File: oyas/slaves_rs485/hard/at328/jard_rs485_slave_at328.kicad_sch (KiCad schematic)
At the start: 60 parts, among them J1 POWER, J7 ISCP, U1 BPC_Alim5V, U1 MAX485E, U2 ATmega328P-A, Y1 8MHz

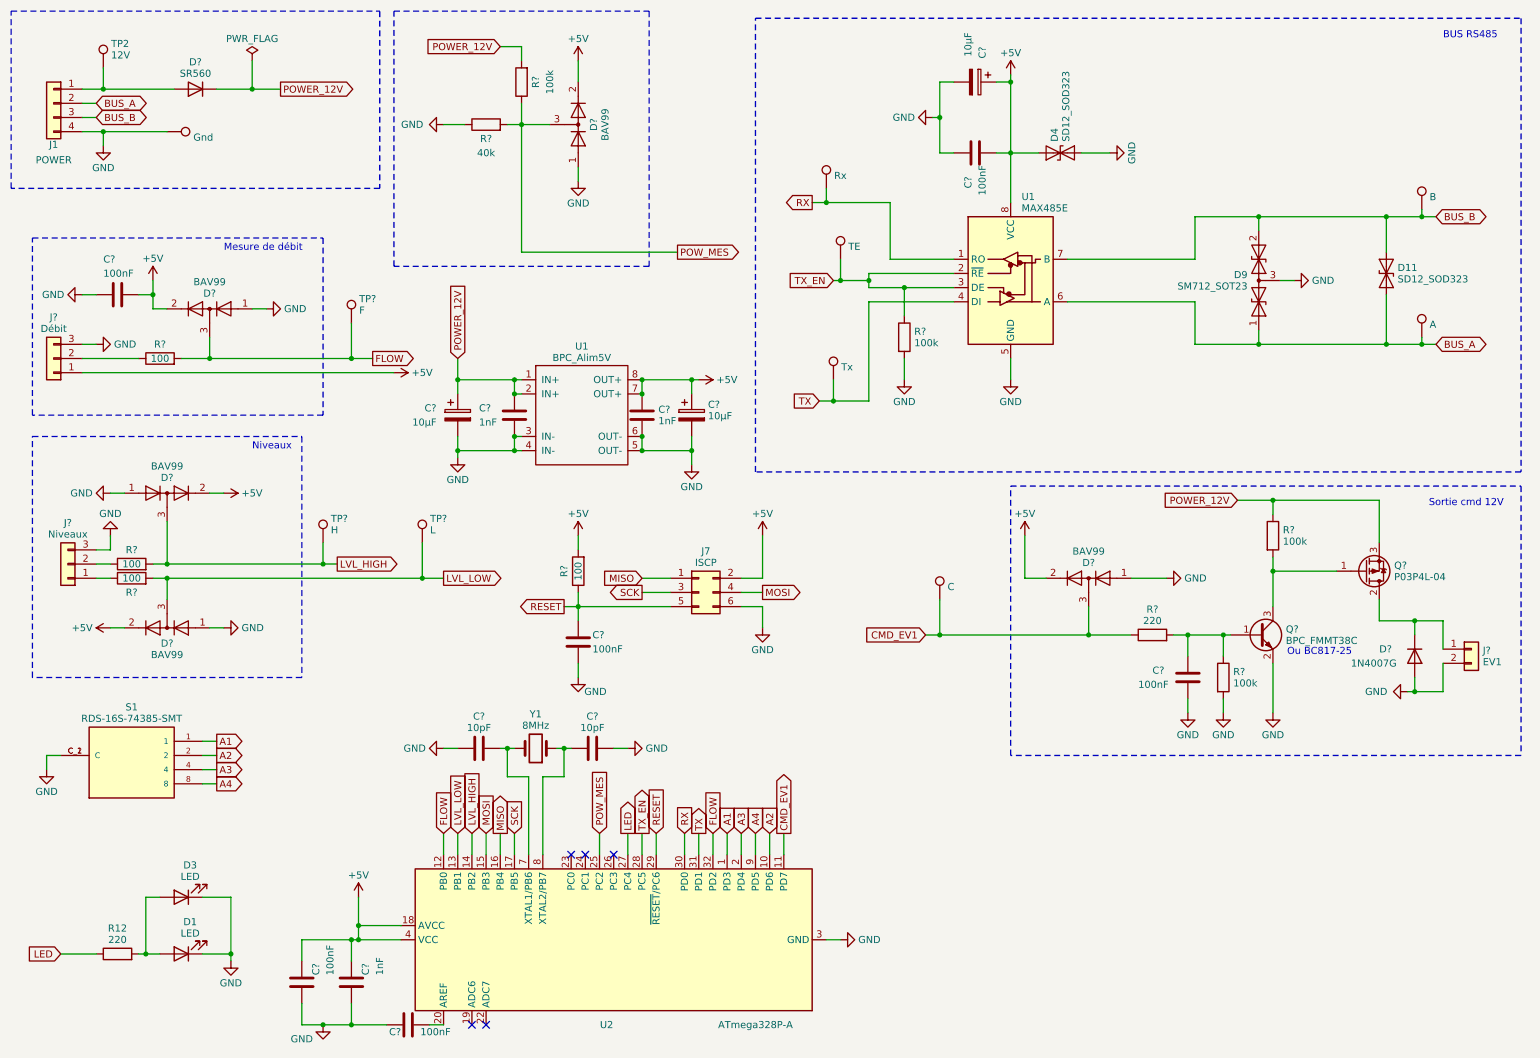
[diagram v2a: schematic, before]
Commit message: Améliorations sur carte AT328
- Capas en hand soldering et en 805
- TP + gros
- Repères composants
- Carte moins longue
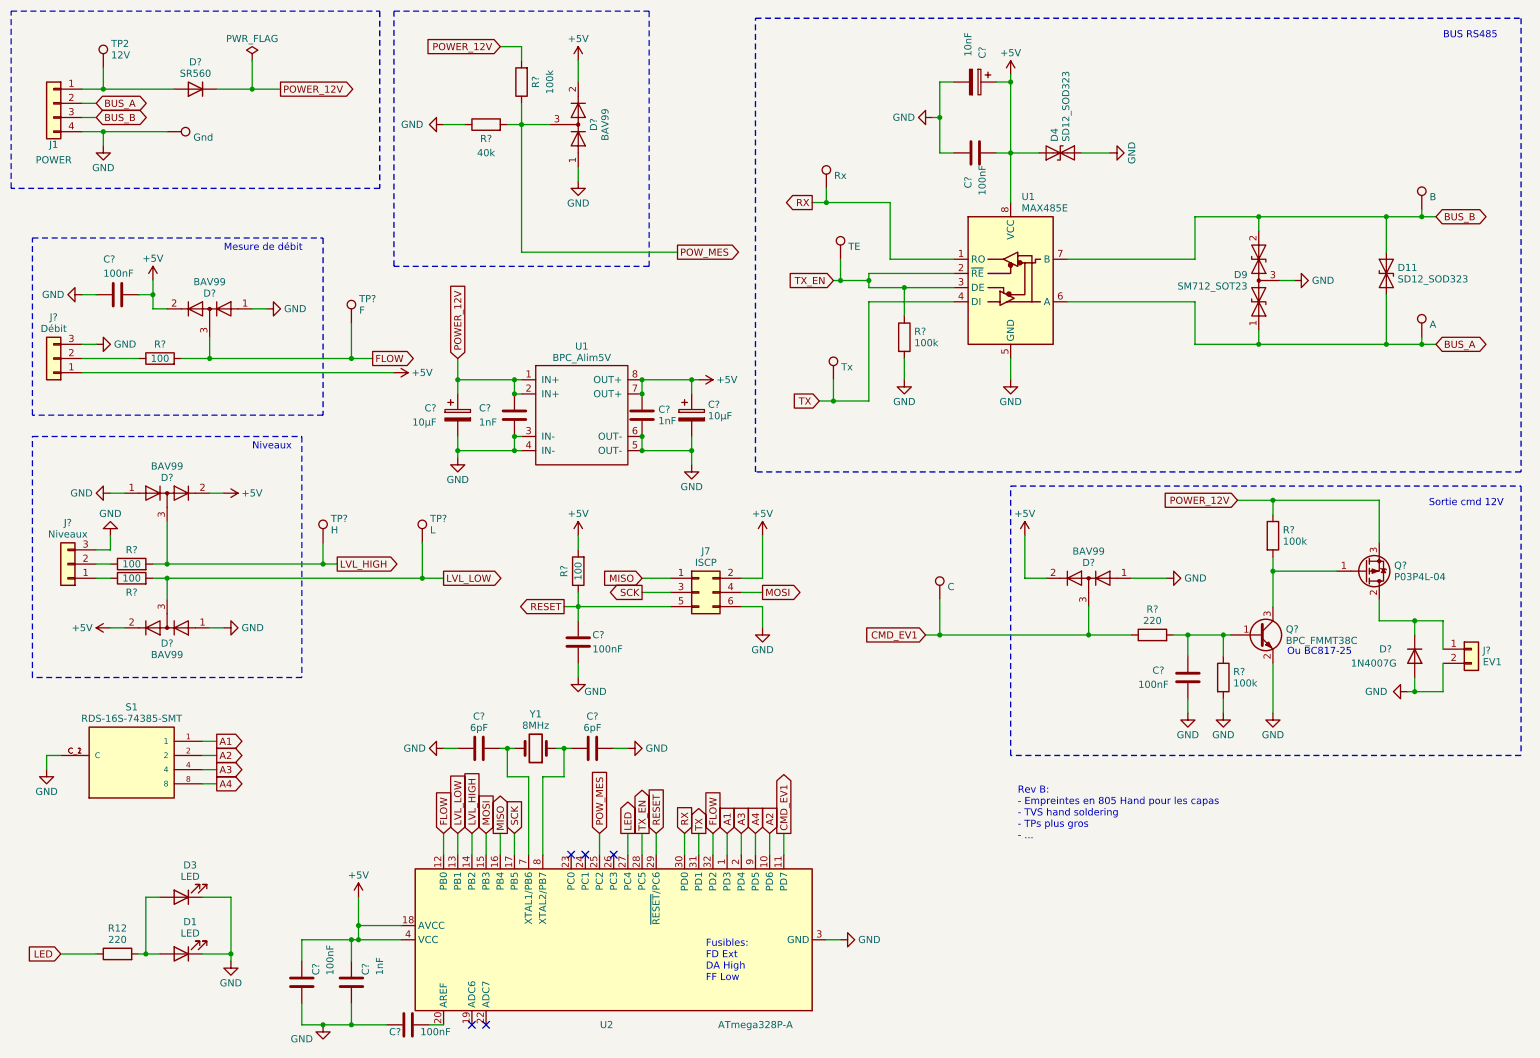
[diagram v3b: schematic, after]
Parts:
- C? (x6): footprint Capacitor_SMD:C_0805_2012Metric -> Capacitor_SMD:C_0805_2012Metric_Pad1.18x1.45mm_HandSolder
- C? (x2): footprint Capacitor_SMD:C_0603_1608Metric -> Capacitor_SMD:C_0805_2012Metric_Pad1.18x1.45mm_HandSolder
- C? (x2): value 10pF -> 6pF; footprint Capacitor_SMD:C_0603_1608Metric -> Capacitor_SMD:C_0603_1608Metric_Pad1.08x0.95mm_HandSolder
- C?: value 10µF -> 10nF; footprint Capacitor_SMD:C_0805_2012Metric -> Capacitor_SMD:C_0805_2012Metric_Pad1.18x1.45mm_HandSolder
- TP1, TP2, TP3, TP4, TP5, TP? (x4): footprint TestPoint:TestPoint_Pad_D1.0mm -> TestPoint:TestPoint_Pad_D2.0mm
- U1: Fabricant (none) -> Analog Devices; Fournisseur (none) -> Farnell; RefFabricant (none) -> MAX485ESA+; RefFournisseur (none) -> 2519382
- U2: Fabricant (none) -> MICROCHIP; Fournisseur (none) -> Farnell; RefFabricant (none) -> ATMEGA328P-AU; RefFournisseur (none) -> 1715486
- Y1: Fabricant (none) -> Abracon; Farnel 4242855 -> (none); Fournisseur (none) -> Farnell; RefFab ABM8AAIG-8.000MHZ-V2R-T3 -> (none); RefFabricant (none) -> ABM8AAIG-8.000MHZ-V2R-T3; RefFournisseur (none) -> 4242855
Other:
- note added: "Fusibles: FD Ext DA High FF Low"
- note added: "Rev B: - Empreintes en 805 Hand pour les capas - TVS hand soldering - TPs plus gros - ..."
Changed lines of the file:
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@@
     (effects (font (size 1.27 1.27)) (justify left bottom))
   )
+  (text "Fusibles:\nFD Ext\nDA High\nFF Low" (at 137.16 186.69 0)
+    (effects (font (size 1.27 1.27)) (justify left bottom))
+  )
   (text "Sortie cmd 12V" (at 266.7 101.6 0)
     (effects (font (size 1.27 1.27)) (justify left bottom))
@@
     (effects (font (size 1.27 1.27)) (justify left bottom))
   )
+  (text "Rev B:\n- Empreintes en 805 Hand pour les capas\n- TVS hand soldering\n- TPs plus gros\n- ..."
+    (at 193.04 161.29 0)
+    (effects (font (size 1.27 1.27)) (justify left bottom))
+  )
   (global_label "LED" (shape output) (at 123.19 160.02 90) (fields_autoplaced)
     (effects (font (size 1.27 1.27)) (justify left))
@@
       (effects (font (size 1.27 1.27)) (justify left))
     )
-    (property "Footprint" "Capacitor_SMD:C_0805_2012Metric" (at 87.63 193.3448 0)
+    (property "Footprint" "Capacitor_SMD:C_0805_2012Metric_Pad1.18x1.45mm_HandSolder" (at 87.63 193.3448 0)
       (effects (font (size 1.27 1.27)) hide)
     )
@@
       (effects (font (size 1.27 1.27)) (justify left))
     )
-    (property "Footprint" "Capacitor_SMD:C_0805_2012Metric" (at 224.4852 135.89 0)
+    (property "Footprint" "Capacitor_SMD:C_0805_2012Metric_Pad1.18x1.45mm_HandSolder" (at 224.4852 135.89 0)
       (effects (font (size 1.27 1.27)) hide)
     )
@@
       (effects (font (size 1.27 1.27)) (justify left))
     )
-    (property "Footprint" "TestPoint:TestPoint_Pad_D1.0mm" (at 78.74 68.58 0)
+    (property "Footprint" "TestPoint:TestPoint_Pad_D2.0mm" (at 78.74 68.58 0)
       (effects (font (size 1.27 1.27)) hide)
     )
@@
       (effects (font (size 1.27 1.27)) (justify left))
     )
-    (property "Footprint" "Capacitor_SMD:C_0805_2012Metric" (at 115.2652 129.54 0)
+    (property "Footprint" "Capacitor_SMD:C_0805_2012Metric_Pad1.18x1.45mm_HandSolder" (at 115.2652 129.54 0)
       (effects (font (size 1.27 1.27)) hide)
     )
@@
       (effects (font (size 1.27 1.27)) (justify left))
     )
-    (property "Footprint" "Capacitor_SMD:C_0805_2012Metric" (at 65.7352 190.5 0)
+    (property "Footprint" "Capacitor_SMD:C_0805_2012Metric_Pad1.18x1.45mm_HandSolder" (at 65.7352 190.5 0)
       (effects (font (size 1.27 1.27)) hide)
     )
@@
       (effects (font (size 1.27 1.27)) (justify left))
     )
-    (property "Footprint" "Capacitor_SMD:C_0603_1608Metric" (at 126.6952 88.9 0)
+    (property "Footprint" "Capacitor_SMD:C_0805_2012Metric_Pad1.18x1.45mm_HandSolder" (at 126.6952 88.9 0)
       (effects (font (size 1.27 1.27)) hide)
     )
@@
       (effects (font (size 1.27 1.27)) (justify left))
     )
-    (property "Footprint" "TestPoint:TestPoint_Pad_D1.0mm" (at 165.1 78.74 0)
+    (property "Footprint" "TestPoint:TestPoint_Pad_D2.0mm" (at 165.1 78.74 0)
       (effects (font (size 1.27 1.27)) hide)
     )
@@
       (effects (font (size 1.27 1.27)) (justify left))
     )
-    (property "Footprint" "TestPoint:TestPoint_Pad_D1.0mm" (at 34.29 22.86 0)
+    (property "Footprint" "TestPoint:TestPoint_Pad_D2.0mm" (at 34.29 22.86 0)
       (effects (font (size 1.27 1.27)) hide)
     )
@@
       (effects (font (size 1.27 1.27)) (justify left))
     )
-    (property "Footprint" "TestPoint:TestPoint_Pad_D1.0mm" (at 91.44 107.95 0)
+    (property "Footprint" "TestPoint:TestPoint_Pad_D2.0mm" (at 91.44 107.95 0)
       (effects (font (size 1.27 1.27)) hide)
     )
@@
       (effects (font (size 1.27 1.27)) (justify left))
     )
-    (property "Footprint" "TestPoint:TestPoint_Pad_D1.0mm" (at 40.64 39.37 0)
+    (property "Footprint" "TestPoint:TestPoint_Pad_D2.0mm" (at 40.64 39.37 0)
       (effects (font (size 1.27 1.27)) hide)
     )
@@
       (effects (font (size 1.27 1.27)) (justify left))
     )
-    (property "Footprint" "TestPoint:TestPoint_Pad_D1.0mm" (at 73.66 107.95 0)
+    (property "Footprint" "TestPoint:TestPoint_Pad_D2.0mm" (at 73.66 107.95 0)
       (effects (font (size 1.27 1.27)) hide)
     )
@@
       (effects (font (size 1.27 1.27)) (justify left))
     )
-    (property "Footprint" "TestPoint:TestPoint_Pad_D1.0mm" (at 270.51 71.12 0)
+    (property "Footprint" "TestPoint:TestPoint_Pad_D2.0mm" (at 270.51 71.12 0)
       (effects (font (size 1.27 1.27)) hide)
     )
@@
       (effects (font (size 1.27 1.27)))
     )
-    (property "Value" "10pF" (at 96.52 141.089 90)
+    (property "Value" "6pF" (at 96.52 141.089 90)
       (effects (font (size 1.27 1.27)))
     )
-    (property "Footprint" "Capacitor_SMD:C_0603_1608Metric" (at 100.33 143.8148 0)
+    (property "Footprint" "Capacitor_SMD:C_0603_1608Metric_Pad1.08x0.95mm_HandSolder" (at 100.33 143.8148 0)
       (effects (font (size 1.27 1.27)) hide)
     )
@@
       (effects (font (size 1.27 1.27)) hide)
     )
+    (property "Fabricant" "MICROCHIP" (at 120.65 179.07 0)
+      (effects (font (size 1.27 1.27)) hide)
+    )
+    (property "Fournisseur" "Farnell" (at 120.65 179.07 0)
+      (effects (font (size 1.27 1.27)) hide)
+    )
+    (property "RefFabricant" "ATMEGA328P-AU" (at 120.65 179.07 0)
+      (effects (font (size 1.27 1.27)) hide)
+    )
+    (property "RefFournisseur" "1715486" (at 120.65 179.07 0)
+      (effects (font (size 1.27 1.27)) hide)
+    )
     (pin "1")
     (pin "10")
@@
       (effects (font (size 1.27 1.27)) (justify left))
     )
-    (property "Footprint" "TestPoint:TestPoint_Pad_D1.0mm" (at 184.15 118.11 0)
+    (property "Footprint" "TestPoint:TestPoint_Pad_D2.0mm" (at 184.15 118.11 0)
       (effects (font (size 1.27 1.27)) hide)
     )
@@
       (effects (font (size 1.27 1.27)) (justify left))
     )
-    (property "Value" "10µF" (at 184.15 16.51 0)
+    (property "Value" "10nF" (at 184.15 16.51 0)
       (effects (font (size 1.27 1.27)) (justify left))
     )
-    (property "Footprint" "Capacitor_SMD:C_0805_2012Metric" (at 181.61 26.3652 0)
+    (property "Footprint" "Capacitor_SMD:C_0805_2012Metric_Pad1.18x1.45mm_HandSolder" (at 181.61 26.3652 0)
       (effects (font (size 1.27 1.27)) hide)
     )
@@
       (effects (font (size 1.27 1.27)) (justify left))
     )
-    (property "Footprint" "TestPoint:TestPoint_Pad_D1.0mm" (at 270.51 48.26 0)
+    (property "Footprint" "TestPoint:TestPoint_Pad_D2.0mm" (at 270.51 48.26 0)
       (effects (font (size 1.27 1.27)) hide)
     )
@@
       (effects (font (size 1.27 1.27)) hide)
     )
-    (property "Farnel" "4242855" (at 106.68 151.13 0)
+    (property "RefFournisseur" "4242855" (at 106.68 151.13 0)
       (effects (font (size 1.27 1.27)) hide)
     )
-    (property "RefFab" "ABM8AAIG-8.000MHZ-V2R-T3" (at 108.728 141.4526 90)
-      (effects (font (size 1.27 1.27)) (justify right) hide)
+    (property "RefFabricant" "ABM8AAIG-8.000MHZ-V2R-T3" (at 105.41 135.89 0)
+      (effects (font (size 1.27 1.27)) hide)
+    )
+    (property "Fabricant" "Abracon" (at 106.68 144.78 0)
+      (effects (font (size 1.27 1.27)) hide)
+    )
+    (property "Fournisseur" "Farnell" (at 106.68 144.78 0)
+      (effects (font (size 1.27 1.27)) hide)
     )
     (pin "1")
@@
       (effects (font (size 1.27 1.27)) (justify left))
     )
-    (property "Footprint" "TestPoint:TestPoint_Pad_D1.0mm" (at 166.37 57.15 0)
+    (property "Footprint" "TestPoint:TestPoint_Pad_D2.0mm" (at 166.37 57.15 0)
       (effects (font (size 1.27 1.27)) hide)
     )
@@
       (effects (font (size 1.27 1.27)) hide)
     )
+    (property "Fabricant" "Analog Devices" (at 191.77 59.69 0)
+      (effects (font (size 1.27 1.27)) hide)
+    )
+    (property "Fournisseur" "Farnell" (at 191.77 59.69 0)
+      (effects (font (size 1.27 1.27)) hide)
+    )
+    (property "RefFabricant" "MAX485ESA+" (at 191.77 59.69 0)
+      (effects (font (size 1.27 1.27)) hide)
+    )
+    (property "RefFournisseur" "2519382" (at 191.77 59.69 0)
+      (effects (font (size 1.27 1.27)) hide)
+    )
     (pin "1")
     (pin "2")
@@
       (effects (font (size 1.27 1.27)) (justify left))
     )
-    (property "Footprint" "Capacitor_SMD:C_0805_2012Metric" (at 189.23 37.1348 0)
+    (property "Footprint" "Capacitor_SMD:C_0805_2012Metric_Pad1.18x1.45mm_HandSolder" (at 189.23 37.1348 0)
       (effects (font (size 1.27 1.27)) hide)
     )
@@
       (effects (font (size 1.27 1.27)) (justify left))
     )
-    (property "Footprint" "Capacitor_SMD:C_0805_2012Metric" (at 27.94 64.4652 0)
+    (property "Footprint" "Capacitor_SMD:C_0805_2012Metric_Pad1.18x1.45mm_HandSolder" (at 27.94 64.4652 0)
       (effects (font (size 1.27 1.27)) hide)
     )
@@
       (effects (font (size 1.27 1.27)))
     )
-    (property "Value" "10pF" (at 116.84 141.089 90)
+    (property "Value" "6pF" (at 116.84 141.089 90)
       (effects (font (size 1.27 1.27)))
     )
-    (property "Footprint" "Capacitor_SMD:C_0603_1608Metric" (at 120.65 143.8148 0)
+    (property "Footprint" "Capacitor_SMD:C_0603_1608Metric_Pad1.08x0.95mm_HandSolder" (at 120.65 143.8148 0)
       (effects (font (size 1.27 1.27)) hide)
     )
@@
       (effects (font (size 1.27 1.27)) (justify left))
     )
-    (property "Footprint" "TestPoint:TestPoint_Pad_D1.0mm" (at 163.83 44.45 0)
+    (property "Footprint" "TestPoint:TestPoint_Pad_D2.0mm" (at 163.83 44.45 0)
       (effects (font (size 1.27 1.27)) hide)
     )
@@
       (effects (font (size 1.27 1.27)) (justify left))
     )
-    (property "Footprint" "Capacitor_SMD:C_0603_1608Metric" (at 103.8352 88.9 0)
+    (property "Footprint" "Capacitor_SMD:C_0805_2012Metric_Pad1.18x1.45mm_HandSolder" (at 103.8352 88.9 0)
       (effects (font (size 1.27 1.27)) hide)
     )
